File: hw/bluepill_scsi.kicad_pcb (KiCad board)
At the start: 2 copper layers, 43.8 x 73.7 mm, 90 parts, among them J2 Conn_01x04_Male, J3 USB_B_Micro, J4 Berg Power Connector, J5 Conn_02x25_Odd_Even, J6 Micro_SD_Card, J7 Conn_02x03_Odd_Even, J8 Conn_01x04_Male, SW1 SW_Push, U1 MIC5504-3.3YM5, U2 STM32F103C8Tx, U3 BluePill_STM32F103C, Y2 8MHz, Y3 32.768k

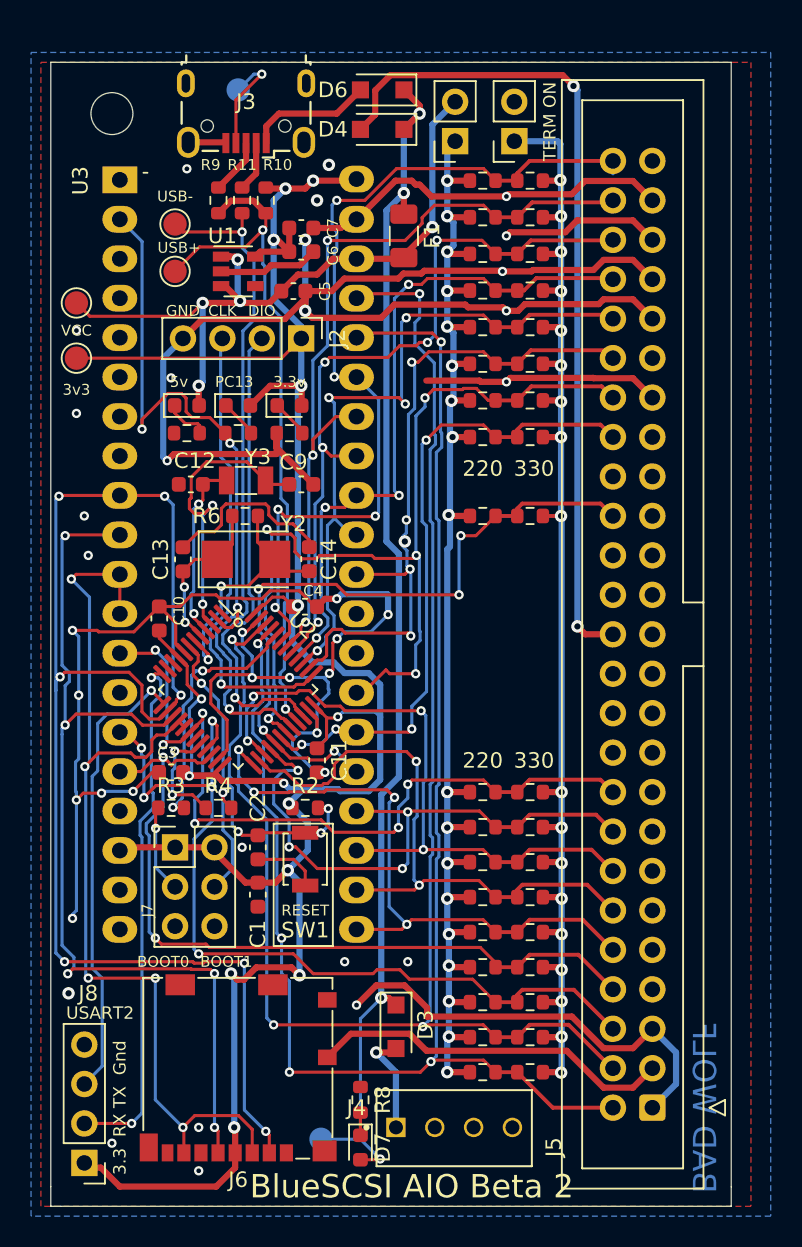
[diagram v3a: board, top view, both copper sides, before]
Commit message: Fixed resistor sizes. As-ordered Beta 3
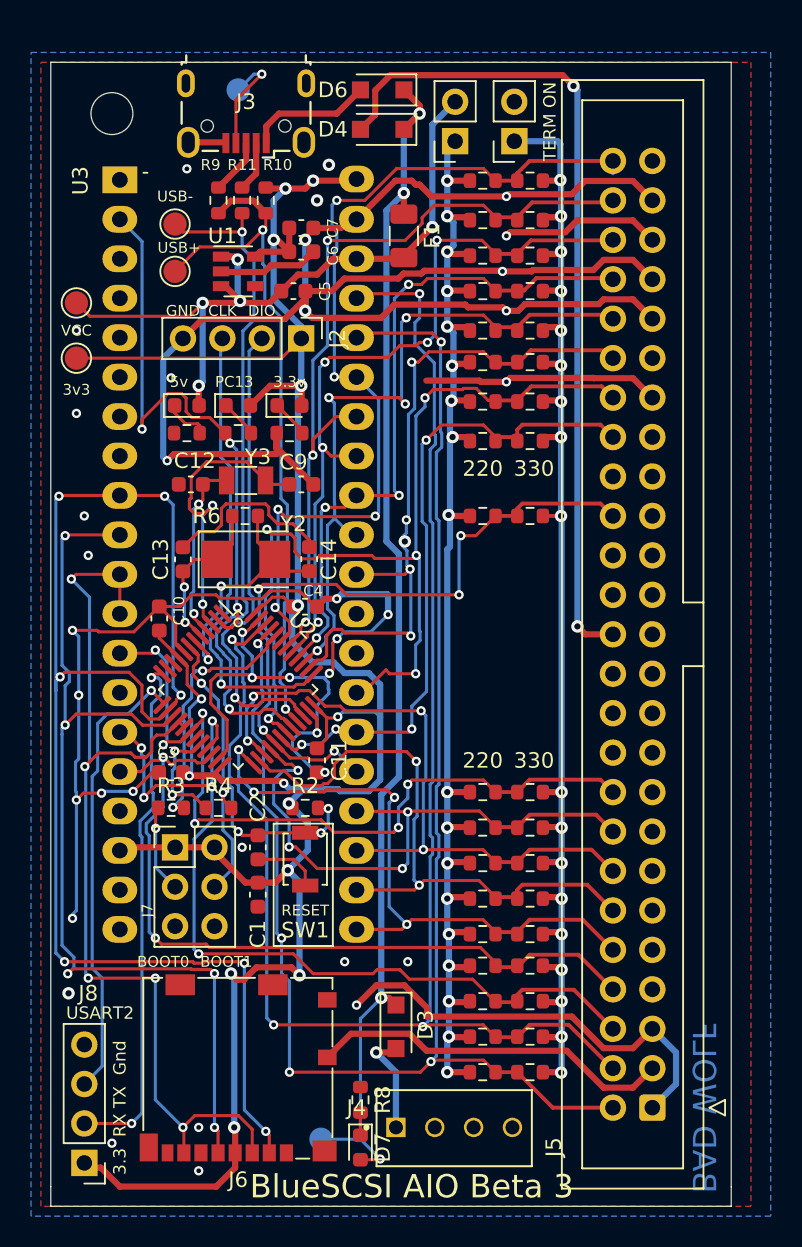
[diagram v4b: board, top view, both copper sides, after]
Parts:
- removed C15, C17, C19, C21, C23, C25, C27, C29, C31, C33, C35, C37, C39, C41, C43, C45, C47, C49: 330, Resistor_SMD:R_0603_1608Metric
- removed C16, C18, C20, C22, C24, C26, C28, C30, C32, C34, C36, C38, C40, C42, C44, C46, C48, C8: 220, Resistor_SMD:R_0603_1608Metric
- added R12: 220, Resistor_SMD:R_0603_1608Metric, F.Cu at (98.9, 83.2)
- added R13: 330, Resistor_SMD:R_0603_1608Metric, F.Cu at (102.0, 83.2)
- added R14: 220, Resistor_SMD:R_0603_1608Metric, F.Cu at (98.9, 85.7)
- added R15: 330, Resistor_SMD:R_0603_1608Metric, F.Cu at (102.0, 85.7)
- added R16: 220, Resistor_SMD:R_0603_1608Metric, F.Cu at (98.9, 88.0)
- added R17: 330, Resistor_SMD:R_0603_1608Metric, F.Cu at (102.0, 88.0)
- added R18: 220, Resistor_SMD:R_0603_1608Metric, F.Cu at (98.9, 92.8)
- added R19: 330, Resistor_SMD:R_0603_1608Metric, F.Cu at (102.0, 92.8)
- added R20: 220, Resistor_SMD:R_0603_1608Metric, F.Cu at (98.9, 99.9)
- added R21: 330, Resistor_SMD:R_0603_1608Metric, F.Cu at (102.0, 99.9)
- added R22: 220, Resistor_SMD:R_0603_1608Metric, F.Cu at (98.9, 90.3)
- added R23: 330, Resistor_SMD:R_0603_1608Metric, F.Cu at (102.0, 90.3)
- added R24: 220, Resistor_SMD:R_0603_1608Metric, F.Cu at (98.9, 94.9)
- added R25: 330, Resistor_SMD:R_0603_1608Metric, F.Cu at (102.0, 94.9)
- added R26: 220, Resistor_SMD:R_0603_1608Metric, F.Cu at (98.9, 97.4)
- added R27: 330, Resistor_SMD:R_0603_1608Metric, F.Cu at (102.0, 97.4)
- added R28: 220, Resistor_SMD:R_0603_1608Metric, F.Cu at (98.9, 104.8)
- added R29: 330, Resistor_SMD:R_0603_1608Metric, F.Cu at (102.0, 104.8)
- added R30: 220, Resistor_SMD:R_0603_1608Metric, F.Cu at (98.9, 122.6)
- added R31: 330, Resistor_SMD:R_0603_1608Metric, F.Cu at (102.0, 122.6)
- added R32: 220, Resistor_SMD:R_0603_1608Metric, F.Cu at (98.9, 140.6)
- added R33: 330, Resistor_SMD:R_0603_1608Metric, F.Cu at (102.0, 140.6)
- added R34: 220, Resistor_SMD:R_0603_1608Metric, F.Cu at (98.9, 138.3)
- added R35: 330, Resistor_SMD:R_0603_1608Metric, F.Cu at (102.0, 138.3)
- added R36: 220, Resistor_SMD:R_0603_1608Metric, F.Cu at (98.9, 136.0)
- added R37: 330, Resistor_SMD:R_0603_1608Metric, F.Cu at (102.0, 136.0)
- added R38: 220, Resistor_SMD:R_0603_1608Metric, F.Cu at (98.9, 133.7)
- added R39: 330, Resistor_SMD:R_0603_1608Metric, F.Cu at (102.0, 133.7)
- added R40: 220, Resistor_SMD:R_0603_1608Metric, F.Cu at (98.9, 131.7)
- added R41: 330, Resistor_SMD:R_0603_1608Metric, F.Cu at (102.0, 131.7)
- added R42: 220, Resistor_SMD:R_0603_1608Metric, F.Cu at (98.9, 129.4)
- added R43: 330, Resistor_SMD:R_0603_1608Metric, F.Cu at (102.0, 129.4)
- added R44: 220, Resistor_SMD:R_0603_1608Metric, F.Cu at (98.9, 127.1)
- added R45: 330, Resistor_SMD:R_0603_1608Metric, F.Cu at (102.0, 127.1)
- added R46: 220, Resistor_SMD:R_0603_1608Metric, F.Cu at (98.9, 124.8)
- added R47: 330, Resistor_SMD:R_0603_1608Metric, F.Cu at (102.0, 124.8)
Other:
- board text added: "BlueSCSI AIO Beta 3"
- board text removed: "BlueSCSI AIO Beta 2"

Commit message: Fixes from integration. As-ordered 1.0
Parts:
- removed D7: LED_Small, LED_SMD:LED_0603_1608Metric
- removed F1: 1A, Fuse:Fuse_1206_3216Metric
- removed J7: Conn_02x03_Odd_Even, Connector_PinHeader_2.54mm:PinHeader_2x03_P2.54mm_Vertical
- removed JP1: TERM_ENABLE_GND, Connector_PinSocket_2.54mm:PinSocket_1x02_P2.54mm_Vertical
- removed JP2: TERM_ENABLE_5V, Connector_PinSocket_2.54mm:PinSocket_1x02_P2.54mm_Vertical
- removed R8: 4.7k, Resistor_SMD:R_0603_1608Metric
- added J1: Conn_02x02_Odd_Even, Connector_PinHeader_2.54mm:PinHeader_2x02_P2.54mm_Vertical, F.Cu at (101.8, 78.1)
- added JP3: Jumper_3_Bridged12, Jumper:SolderJumper-3_P1.3mm_Bridged12_RoundedPad1.0x1.5mm, B.Cu at (79.8, 130.1)
- added JP4: Jumper_3_Bridged12, Jumper:SolderJumper-3_P1.3mm_Bridged12_RoundedPad1.0x1.5mm, B.Cu at (79.8, 127.6)
- added TP10: TestPoint_Small, TestPoint:TestPoint_THTPad_D1.0mm_Drill0.5mm, F.Cu at (87.7, 148.0)
- added TP11: TestPoint_Small, TestPoint:TestPoint_THTPad_D1.0mm_Drill0.5mm, F.Cu at (83.5, 148.0)
- added TP12: TestPoint_Small, TestPoint:TestPoint_THTPad_D1.0mm_Drill0.5mm, F.Cu at (79.2, 148.0)
- added TP13: TestPoint_Small, TestPoint:TestPoint_THTPad_D1.0mm_Drill0.5mm, F.Cu at (77.1, 148.0)
- added TP14: TestPoint_Small, TestPoint:TestPoint_Pad_D1.5mm, F.Cu at (72.8, 87.6)
- added TP7: TestPoint_Small, TestPoint:TestPoint_THTPad_D1.0mm_Drill0.5mm, F.Cu at (81.3, 148.0)
- added TP8: TestPoint_Small, TestPoint:TestPoint_THTPad_D1.0mm_Drill0.5mm, F.Cu at (92.0, 148.0)
- added TP9: TestPoint_Small, TestPoint:TestPoint_THTPad_D1.0mm_Drill0.5mm, F.Cu at (89.8, 148.0)
- D3, D4, D6: value SM4007PL -> D_Schottky; footprint Diode_SMD:D_SOD-123F -> Diode_SMD:D_SOD-123
- SW1: footprint Button_Switch_SMD:SW_SPST_B3U-1000P -> Button_Switch_THT:SW_PUSH_6mm
- TP6: footprint TestPoint:TestPoint_Pad_D1.5mm -> TestPoint:TestPoint_THTPad_D1.0mm_Drill0.5mm; moved to F.Cu
- moved D3 59.0 mm to (93.9, 78.6), turned to 90 degrees
- moved C1 33.2 mm to (86.5, 96.0), turned to 180 degrees
- moved R2 6.76 mm to (80.7, 123.8), turned to 90 degrees
- moved C2 6.37 mm to (80.1, 130.8), turned to 180 degrees
- moved TP6 4.26 mm to (85.6, 148.0)
- moved D4 3.99 mm to (96.2, 78.6), turned to 90 degrees
- moved R4 2.70 mm to (79.2, 123.8), turned to 270 degrees
- moved SW1 2.68 mm to (87.8, 124.2), turned to 270 degrees
- moved D6 1.58 mm to (91.5, 78.6), turned to 90 degrees
- moved R3 1.15 mm to (77.7, 123.8), turned to 270 degrees
- moved TP2 0.41 mm to (79.2, 88.6)
- moved TP3 0.41 mm to (79.2, 85.6)
- moved C3 0.24 mm to (78.9, 121.5)
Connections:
- C13 pad 2: Net-(C13-Pad2) -> GND
- C14 pad 2: Net-(C13-Pad2) -> GND
- D3 pad 1: +5V -> VCC
- D4 pad 1: +5V -> VCC
- D6 pad 1: +5V -> VCC
- J6 pad 1: (no net) -> Net-(J6-Pad1)
- J6 pad 3: SD_MISO -> SD_MOSI
- J6 pad 8: (no net) -> Net-(J6-Pad8)
- R3 pad 1: Net-(J7-Pad3) -> /Onboard Blue Pil/BOOT_0
- R3 pad 2: /Onboard Blue Pil/BOOT_0 -> Net-(JP3-Pad2)
- TP6 pad 1: +5V -> +3V3
- U2 pad 17: SD_MISO -> SD_MOSI
- U3 pad 12: SD_MISO -> SD_MOSI
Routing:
- net GND: track 288.8 -> 378.7 mm, vias 39 -> 42
- net +5V: track 80.0 -> 0.00 mm, vias 4 -> 0
- net SD_MOSI: track 0.00 -> 64.9 mm, vias 0 -> 6
- net /BERG_5V: track 6.73 -> 68.4 mm
- net Net-(C13-Pad2): track 11.6 -> 0.00 mm
- net SD_CS: track 86.8 -> 77.9 mm, vias 7 -> 6
- net /TERM_PWR: track 53.8 -> 45.7 mm
- net Net-(JP3-Pad2): track 0.00 -> 7.39 mm, vias 0 -> 3
- net Net-(J6-Pad1): track 0.00 -> 6.60 mm
- net Net-(J7-Pad3): track 5.67 -> 0.00 mm, vias 1 -> 0
- net VCC: track 48.1 -> 53.3 mm, vias 5 -> 6
- net SD_CLK: track 61.8 -> 65.6 mm
- net Net-(JP4-Pad2): track 8.00 -> 4.49 mm
- net SCSI_DATP: track 50.8 -> 54.3 mm
- net /Onboard Blue Pil/Reset: track 21.4 -> 24.8 mm, vias 4 -> 1
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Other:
- board text added: "BlueSCSI All-In-One v1.0"
- board text added: "Boot 0"
- board text added: "Boot 1"
- board text added: "CS"
- board text added: "MISO"
- board text added: "MOSI"
- board text removed: "BlueSCSI AIO Beta 3"
